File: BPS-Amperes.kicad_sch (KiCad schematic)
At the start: 35 parts, among them J1 Conn_02x10_Odd_Even, J2 ShuntConn, J3 PassthroughConn, J4 TestConn, J5 Conn_01x02, U1 INA186A3IDDFT, U2 OPA2196, U4 REF1930AIDDCT

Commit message: Flipped components to the back
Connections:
- net +1V5: now also J5.1 (Pin_1); no longer J5.2 (Pin_2)
- net +3V0: now also J5.2 (Pin_2); no longer J5.1 (Pin_1)
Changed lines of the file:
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@@
     (effects (font (size 1.27 1.27)) (justify right bottom))
   )
-  (label "VBIAS" (at 113.03 151.765 0) (fields_autoplaced)
+  (label "VBIAS" (at 113.03 149.225 0) (fields_autoplaced)
     (effects (font (size 1.27 1.27)) (justify left bottom))
   )
@@
     (effects (font (size 1.27 1.27)) (justify left bottom))
   )
-  (label "VREF" (at 113.03 149.225 0) (fields_autoplaced)
+  (label "VREF" (at 113.03 151.765 0) (fields_autoplaced)
     (effects (font (size 1.27 1.27)) (justify left bottom))
   )

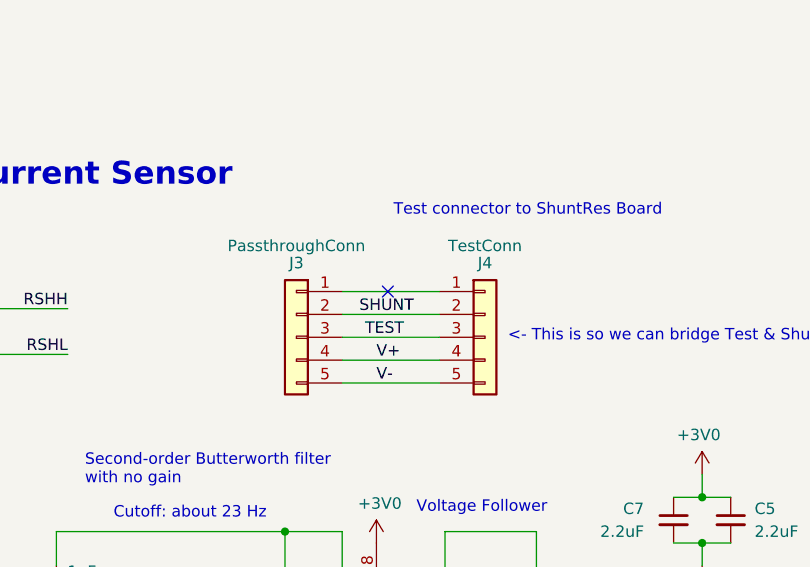
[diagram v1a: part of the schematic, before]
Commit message: adding ground plane to the back
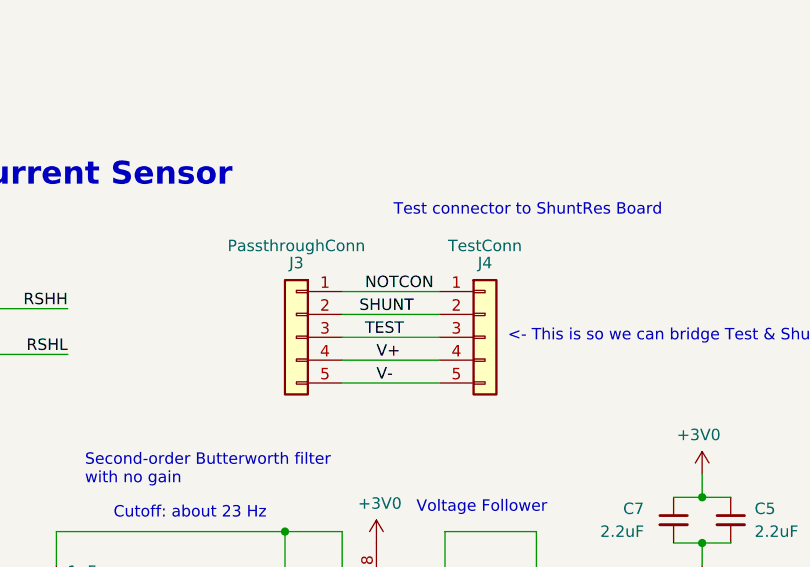
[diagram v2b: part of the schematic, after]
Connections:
- net NOTCON: now reaches J3.1 (Pin_1), J4.1 (Pin_1)
- no-connect marks 15 -> 14
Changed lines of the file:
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@@
   (no_connect (at 239.395 43.18))
   (no_connect (at 257.81 43.18))
-  (no_connect (at 117.475 44.45))
   (no_connect (at 239.395 48.26))
   (no_connect (at 257.81 45.72))
@@
     (effects (font (size 1.27 1.27)) (justify right bottom))
   )
+  (label "NOTCON" (at 114.935 44.45 0) (fields_autoplaced)
+    (effects (font (size 1.27 1.27)) (justify left bottom))
+  )
   (symbol (lib_id "power:GND") (at 146.685 101.6 0) (unit 1)

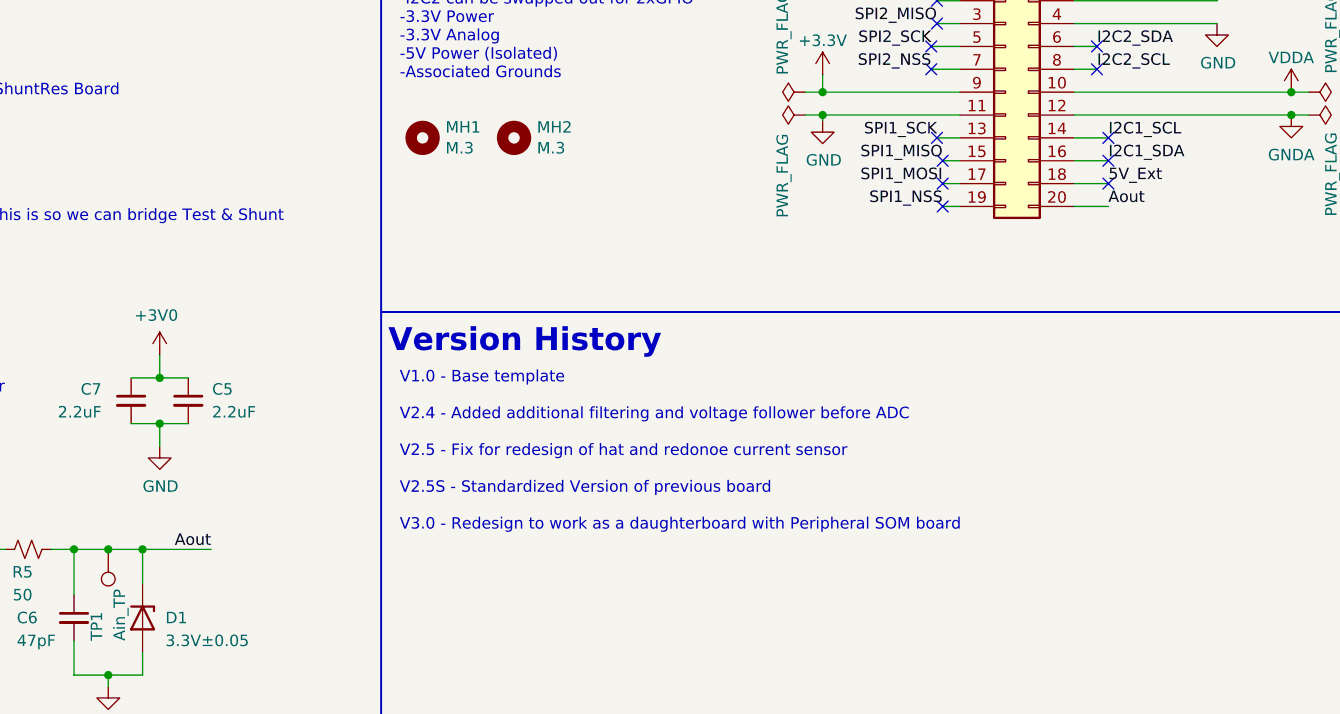
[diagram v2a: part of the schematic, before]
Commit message: Fixed 3.3V Zener & Read Me
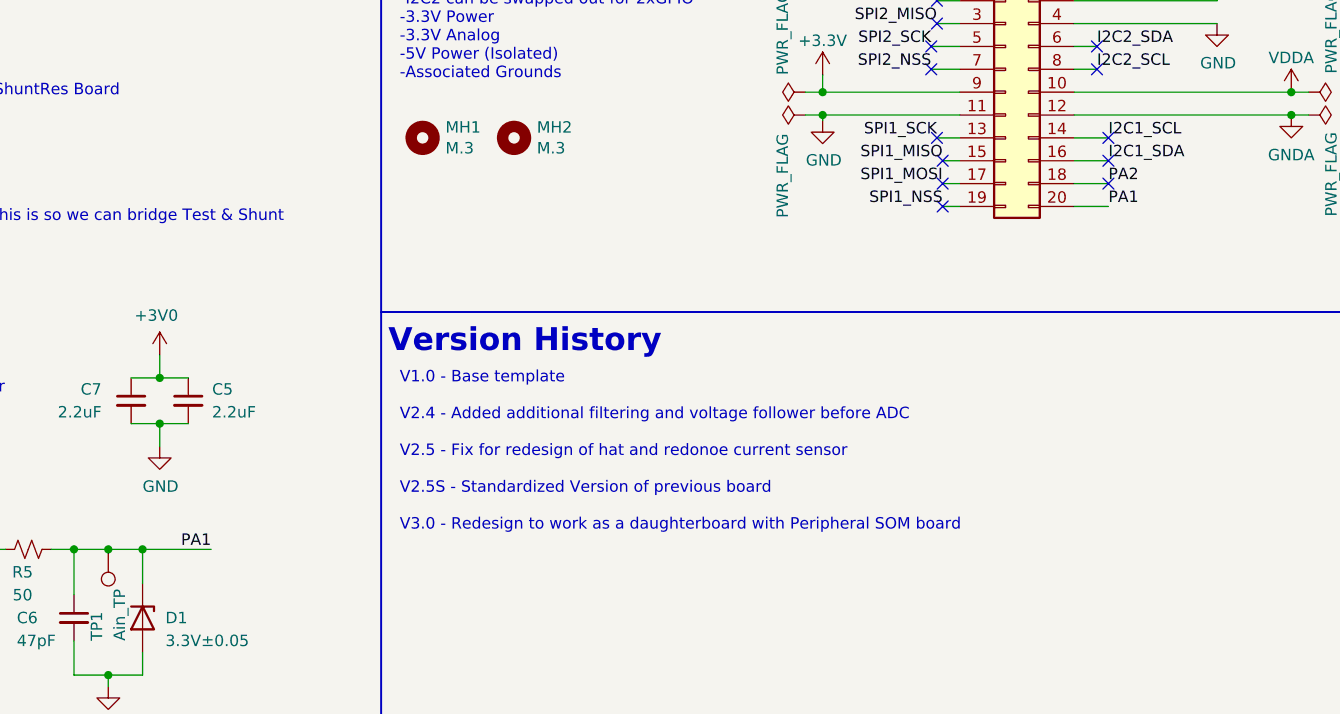
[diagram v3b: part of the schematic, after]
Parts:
- D1: Mfg BZX38450-C3V0X -> 821-BZY55B3V3RBG
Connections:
- net 5V_Ext renamed PA2
- net Aout renamed PA1
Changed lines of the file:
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@@
     (effects (font (size 1.27 1.27)) (justify right bottom))
   )
-  (label "5V_Ext" (at 257.81 45.72 0) (fields_autoplaced)
+  (label "PA2" (at 257.81 45.72 0) (fields_autoplaced)
     (effects (font (size 1.27 1.27)) (justify left bottom))
   )
@@
     (effects (font (size 1.27 1.27)) (justify right bottom))
   )
-  (label "Aout" (at 158.115 86.36 180) (fields_autoplaced)
+  (label "PA1" (at 158.115 86.36 180) (fields_autoplaced)
     (effects (font (size 1.27 1.27)) (justify right bottom))
   )
-  (label "Aout" (at 257.81 48.26 0) (fields_autoplaced)
+  (label "PA1" (at 257.81 48.26 0) (fields_autoplaced)
     (effects (font (size 1.27 1.27)) (justify left bottom))
   )
@@
       (effects (font (size 1.27 1.27)) hide)
     )
-    (property "Datasheet" "~" (at 128.27 49.53 0)
+    (property "Datasheet" "https://www.mouser.com/ProductDetail/Harwin/M20-9960545?qs=ulE8k0yEMYZo%252Bcs6mcbFmQ%3D%3D" (at 128.27 49.53 0)
       (effects (font (size 1.27 1.27)) hide)
     )
@@
       (effects (font (size 1.27 1.27)) hide)
     )
-    (property "Datasheet" "https://www.mouser.com/datasheet/2/916/BZT52H_Q_SER-2721682.pdf" (at 150.495 93.98 0)
-      (effects (font (size 1.27 1.27)) hide)
-    )
-    (property "Mfg" "BZX38450-C3V0X" (at 150.495 93.98 90)
-      (effects (font (size 1.27 1.27)) hide)
-    )
+    (property "Datasheet" "https://www.mouser.com/ProductDetail/Taiwan-Semiconductor/BZY55B3V3-RBG?qs=mAH9sUMRCtvrJdI%2FtfeTug%3D%3D" (at 150.495 93.98 0)
+      (effects (font (size 1.27 1.27)) hide)
+    )
+    (property "Mfg" "821-BZY55B3V3RBG" (at 150.495 93.98 90)
+      (effects (font (size 1.27 1.27)) hide)
+    )

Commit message: Updated Mouser Bom, Added Stitching Vias
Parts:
- C6: Mfg C0805C470JAGACAUTO -> 80-C0805C470JAGAUTO
- D2: Mfg APTD2012LCGCK -> 604-APTD2012LCGCK
- J1: Mfg 53307-2071 -> 538-53307-2071
- R6: Mfg CRCW08051K50JNEB -> 71-CRCW08051K50JNEB
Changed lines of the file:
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@@
       (effects (font (size 1.27 1.27)) hide)
     )
-    (property "Mfg" "C0805C470JAGACAUTO" (at 142.875 93.98 0)
+    (property "Mfg" "80-C0805C470JAGAUTO" (at 142.875 93.98 0)
       (effects (font (size 1.27 1.27)) hide)
     )
@@
       (effects (font (size 1.27 1.27)) hide)
     )
-    (property "Mfg" "53307-2071" (at 246.38 35.56 0)
+    (property "Mfg" "538-53307-2071" (at 246.38 35.56 0)
       (effects (font (size 1.27 1.27)) hide)
     )
@@
       (effects (font (size 1.27 1.27)) hide)
     )
-    (property "Mfg" "CRCW08051K50JNEB" (at 154.305 147.955 0)
+    (property "Mfg" "71-CRCW08051K50JNEB" (at 154.305 147.955 0)
       (effects (font (size 1.27 1.27)) hide)
     )
@@
       (effects (font (size 1.27 1.27)) hide)
     )
-    (property "Mfg" "APTD2012LCGCK" (at 154.305 158.115 90)
-      (effects (font (size 1.27 1.27)) hide)
-    )
+    (property "Mfg" "604-APTD2012LCGCK" (at 154.305 158.115 90)
+      (effects (font (size 1.27 1.27)) hide)
+    )

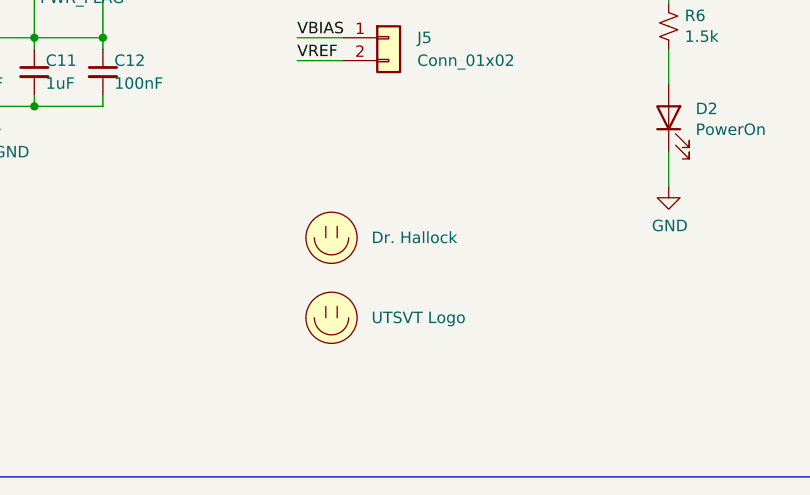
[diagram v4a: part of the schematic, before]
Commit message: Added new logo
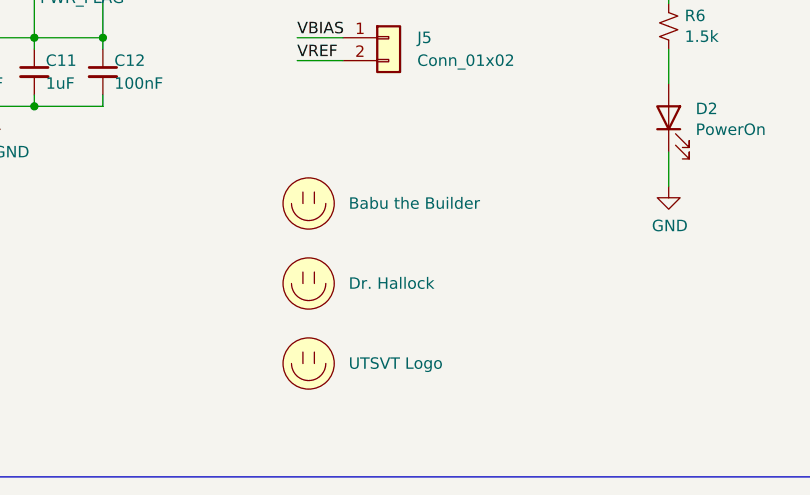
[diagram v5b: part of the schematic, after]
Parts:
- added LOGO2: Babu the Builder, UTSVT_Special:Babu the Builder, symbol utsvt-misc:Logo_Placeholder
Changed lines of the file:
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@@
+    )
+  )
+  (symbol (lib_id "utsvt-misc:Logo_Placeholder") (at 114.3 167.64 0) (unit 1)
+    (in_bom yes) (on_board yes) (dnp no) (fields_autoplaced)
+    (property "Reference" "LOGO2" (at 114.3 163.83 0)
+      (effects (font (size 1.27 1.27)) hide)
+    )
+    (property "Value" "Babu the Builder" (at 118.745 167.64 0)
+      (effects (font (size 1.27 1.27)) (justify left))
+    )
+    (property "Footprint" "UTSVT_Special:Babu the Builder" (at 114.3 165.735 0)
+      (effects (font (size 1.27 1.27)) hide)
+    )
+    (property "Datasheet" "" (at 114.3 165.735 0)
+      (effects (font (size 1.27 1.27)) hide)
+    )
+    (instances
+      (project "BPS-Amperes"
+        (path "/637f68f0-cb9c-412a-8573-5d8e7ef6d8a2"
+          (reference "LOGO2") (unit 1)
+        )
+      )
     )
   )
@@
     )
   )
-  (symbol (lib_id "utsvt-misc:Logo_Placeholder") (at 116.84 180.34 0) (unit 1)
+  (symbol (lib_id "utsvt-misc:Logo_Placeholder") (at 114.3 185.42 0) (unit 1)
     (in_bom yes) (on_board yes) (dnp no) (fields_autoplaced)
-    (property "Reference" "LOGO1" (at 116.84 176.53 0)
-      (effects (font (size 1.27 1.27)) hide)
-    )
-    (property "Value" "UTSVT Logo" (at 121.285 180.34 0)
-      (effects (font (size 1.27 1.27)) (justify left))
-    )
-    (property "Footprint" "UTSVT_Special:UTSVT_Logo_Symbol" (at 116.84 178.435 0)
-      (effects (font (size 1.27 1.27)) hide)
-    )
-    (property "Datasheet" "" (at 116.84 178.435 0)
+    (property "Reference" "LOGO1" (at 114.3 181.61 0)
+      (effects (font (size 1.27 1.27)) hide)
+    )
+    (property "Value" "UTSVT Logo" (at 118.745 185.42 0)
+      (effects (font (size 1.27 1.27)) (justify left))
+    )
+    (property "Footprint" "UTSVT_Special:UTSVT_Logo_Symbol" (at 114.3 183.515 0)
+      (effects (font (size 1.27 1.27)) hide)
+    )
+    (property "Datasheet" "" (at 114.3 183.515 0)
       (effects (font (size 1.27 1.27)) hide)
     )
@@
     )
   )
-  (symbol (lib_id "utsvt-misc:Logo_Placeholder") (at 116.84 171.45 0) (unit 1)
+  (symbol (lib_id "utsvt-misc:Logo_Placeholder") (at 114.3 176.53 0) (unit 1)
     (in_bom yes) (on_board yes) (dnp no) (fields_autoplaced)
-    (property "Reference" "LOGO0" (at 116.84 167.64 0)
-      (effects (font (size 1.27 1.27)) hide)
-    )
-    (property "Value" "Dr. Hallock" (at 121.285 171.45 0)
-      (effects (font (size 1.27 1.27)) (justify left))
-    )
-    (property "Footprint" "UTSVT_Special:Hallock_Image_Tiny" (at 116.84 169.545 0)
-      (effects (font (size 1.27 1.27)) hide)
-    )
-    (property "Datasheet" "" (at 116.84 169.545 0)
-      (effects (font (size 1.27 1.27)) hide)
-    )
+    (property "Reference" "LOGO0" (at 114.3 172.72 0)
+      (effects (font (size 1.27 1.27)) hide)
+    )
+    (property "Value" "Dr. Hallock" (at 118.745 176.53 0)
+      (effects (font (size 1.27 1.27)) (justify left))
+    )
+    (property "Footprint" "UTSVT_Special:Hallock_Image_Tiny" (at 114.3 174.625 0)
+      (effects (font (size 1.27 1.27)) hide)
+    )
+    (property "Datasheet" "" (at 114.3 174.625 0)
+      (effects (font (size 1.27 1.27)) hide)
+    )

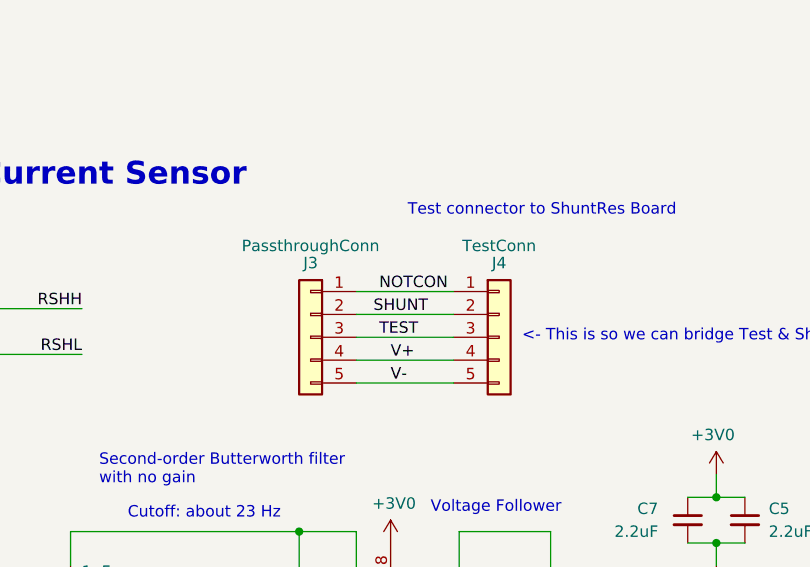
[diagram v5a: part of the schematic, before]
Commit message: Rearranged components and completed initial wiring to route on the front
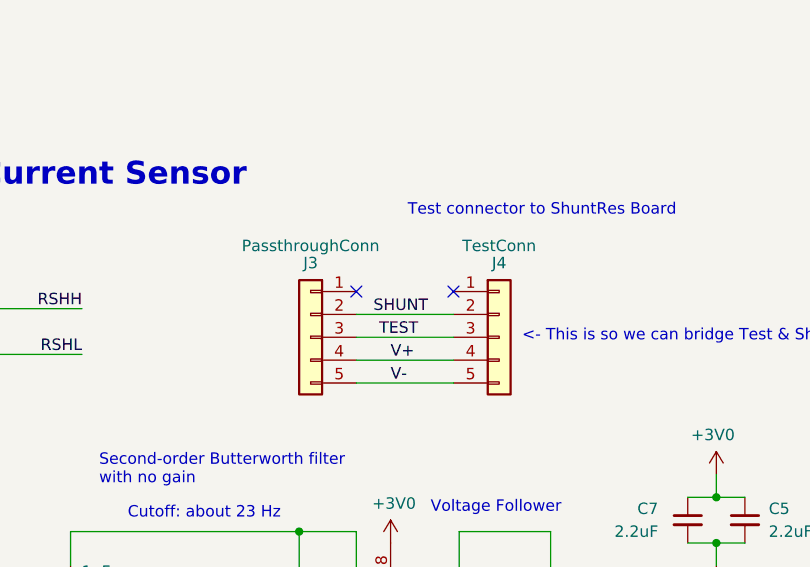
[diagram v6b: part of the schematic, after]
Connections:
- net NOTCON: no longer names the net of J4.1 (Pin_1)
- net NOTCON: no longer J3.1 (Pin_1)
- no-connect marks 14 -> 16
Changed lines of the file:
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@@
   (no_connect (at 238.125 33.02))
   (no_connect (at 239.395 43.18))
+  (no_connect (at 112.395 44.45))
   (no_connect (at 257.81 43.18))
+  (no_connect (at 123.19 44.45))
   (no_connect (at 239.395 48.26))
   (no_connect (at 257.81 45.72))
@@
     (stroke (width 0) (type default))
   )
-  (wire (pts (xy 112.395 44.45) (xy 123.19 44.45))
-    (stroke (width 0) (type default))
-  )
   (wire (pts (xy 238.125 30.48) (xy 241.3 30.48))
     (stroke (width 0) (type default))
@@
     (effects (font (size 1.27 1.27)) (justify right bottom))
   )
-  (label "NOTCON" (at 114.935 44.45 0) (fields_autoplaced)
-    (effects (font (size 1.27 1.27)) (justify left bottom))
-  )
   (symbol (lib_id "power:GND") (at 146.685 101.6 0) (unit 1)
